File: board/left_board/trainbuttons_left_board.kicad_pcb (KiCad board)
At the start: 4 copper layers, 182 x 73 mm, 45 parts, among them J101 USB_C_Receptacle_USB2.0_16P, J102 HDMI_A, J401 UART, J801 DBG, SW201 SW_Push, SW202 SW_Push, SW203 SW_Push, SW204 SW_Push, SW205 SW_Push, SW206 SW_Push, SW207 SW_Push, SW208 SW_Push, SW209 SW_Push, SW210 SW_Push, SW211 SW_Push, SW212 SW_Push, SW213 SW_Push, SW801 RST, U401 STM32G0B0CETx, U501 LM317AEMP, Y601 48MHz

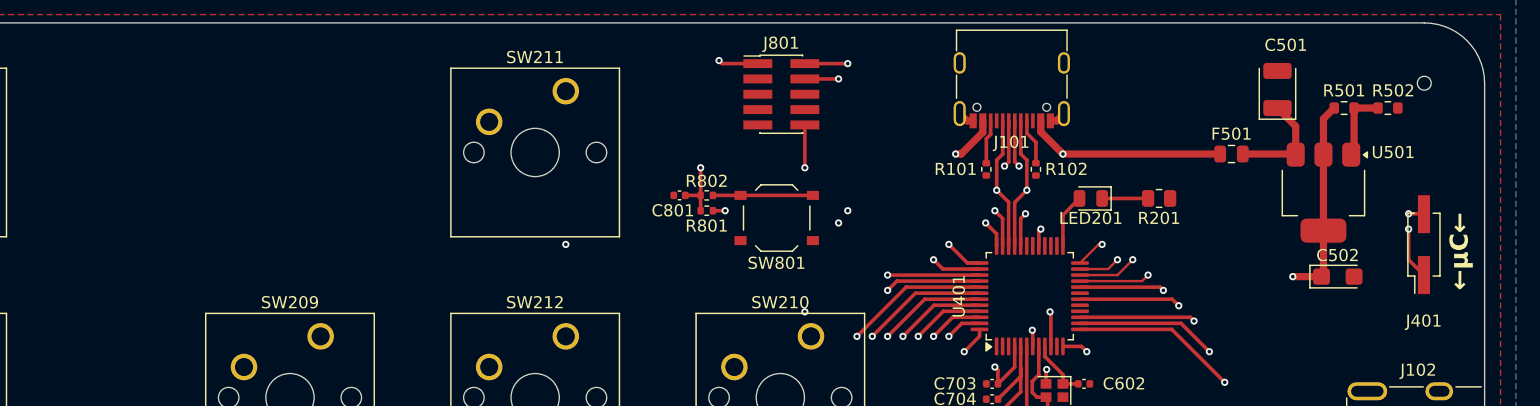
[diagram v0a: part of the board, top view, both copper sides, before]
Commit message: left: replace UART pin header
choose a 2.54mm variant that can be mounted easily
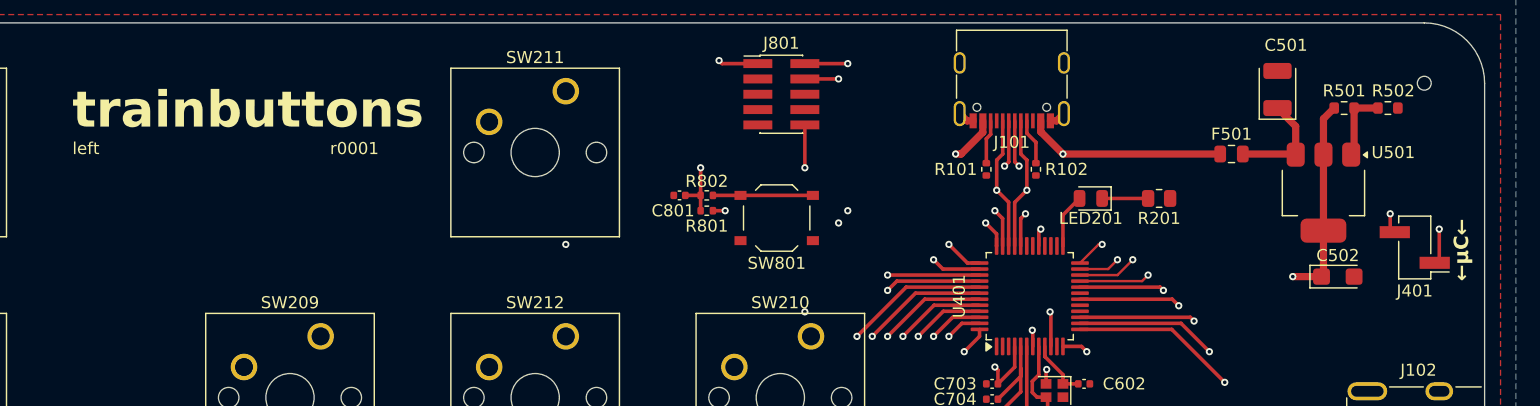
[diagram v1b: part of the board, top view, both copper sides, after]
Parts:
- J401: footprint Connector_PinHeader_2.54mm:PinHeader_2x01_P2.54mm_Vertical_SMD -> Connector_PinHeader_2.54mm:PinHeader_1x02_P2.54mm_Vertical_SMD_Pin1Left
- moved J401 0.80 mm to (206.2, 54.9), turned to 180 degrees
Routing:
- net /MCU/UART_MCURX: track 35.9 -> 34.2 mm
- net /MCU/UART_MCUTX: track 36.3 -> 36.9 mm
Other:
- board text added: "left"
- board text added: "r0001"
- board text added: "trainbuttons"
